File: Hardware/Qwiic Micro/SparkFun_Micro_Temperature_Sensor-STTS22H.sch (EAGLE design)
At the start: 26 parts, among them J1 Qwiic Right Angle, U2 STTS22H

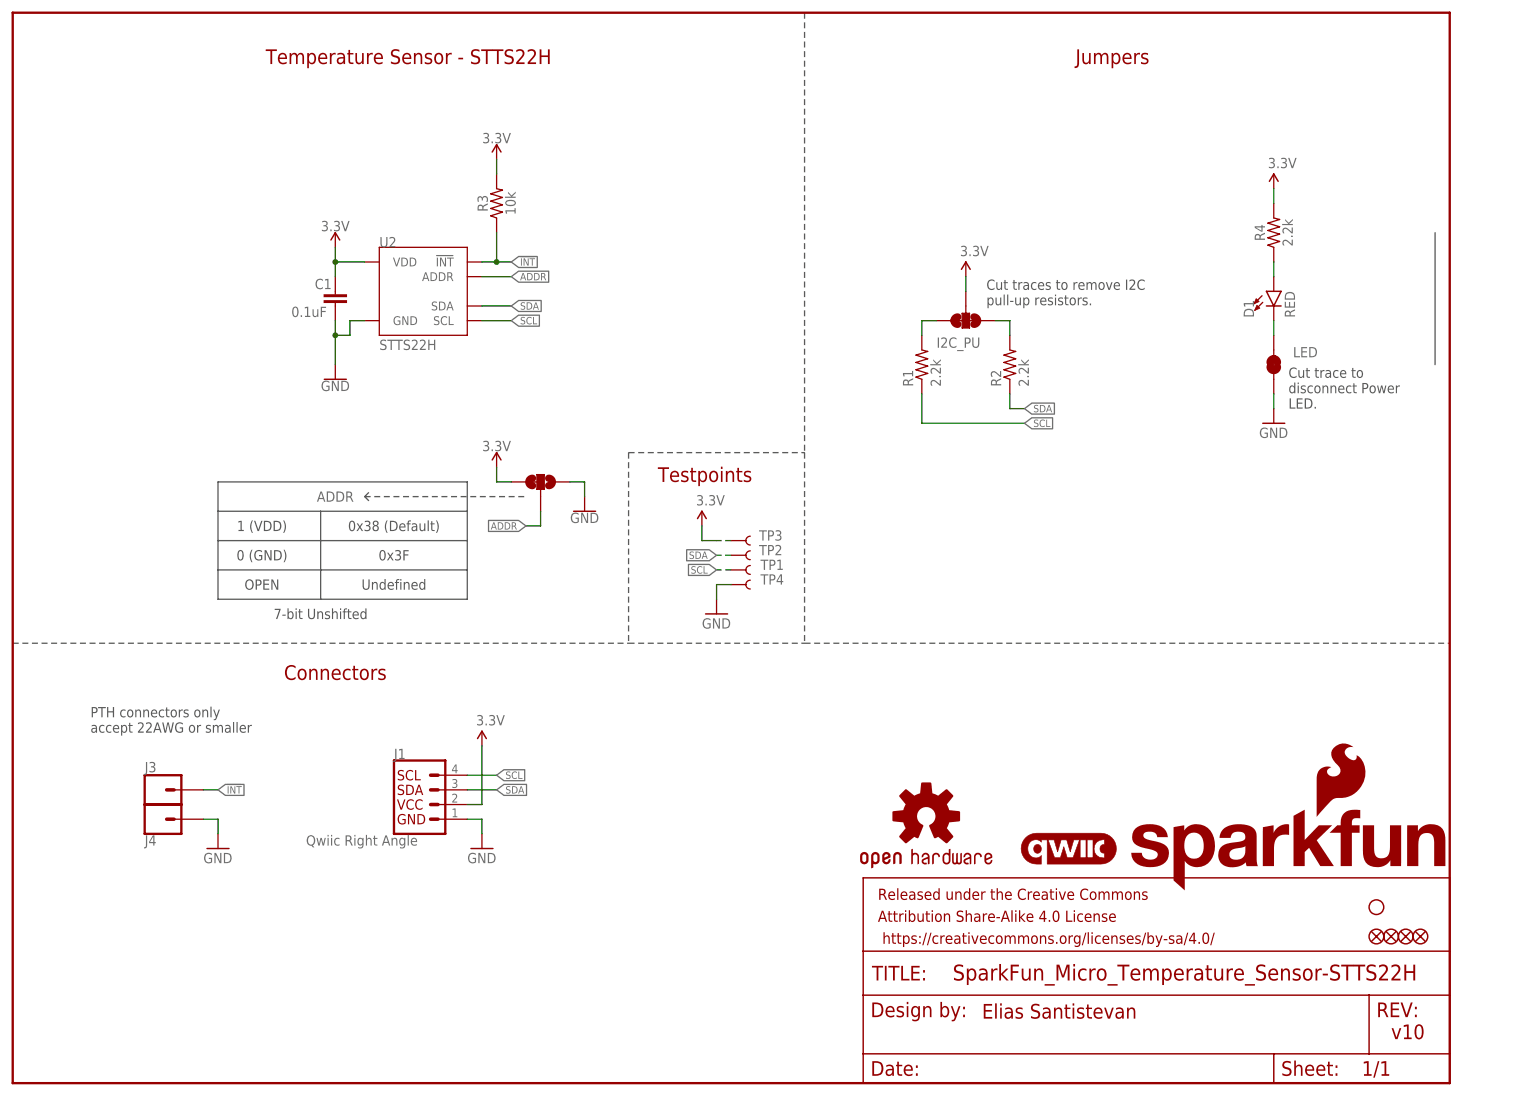
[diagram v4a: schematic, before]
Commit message: Updates temp sensor footprint, Adds bstop underneath IC
* Adds via directly underneath sensor for better temperature sensing
* Fixes various routing inconsistencies
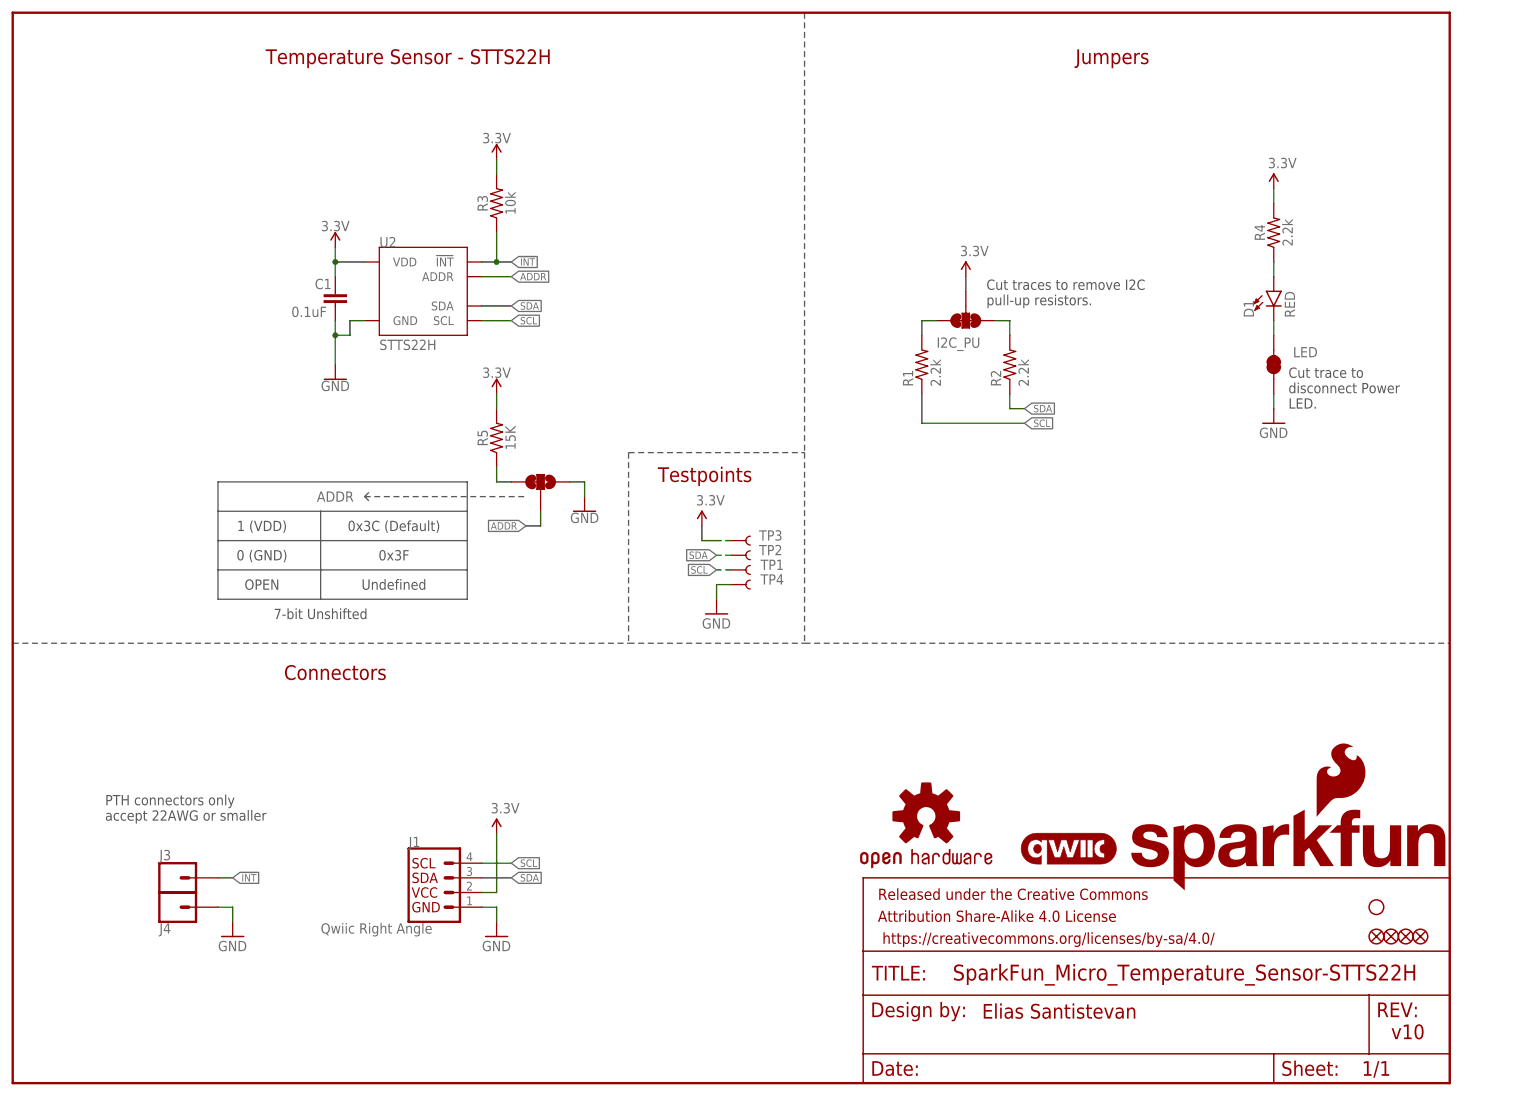
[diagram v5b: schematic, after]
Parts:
- added R5: 15K, SparkFun-Resistors:15KOHM-0402-TIGHT-1/16THW-1%
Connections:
- new net N$1: ADDR.3, R5.1
- net 3.3V: now also R5.2; no longer ADDR.3
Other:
- note added: "0x3C (Default)"
- note removed: "0x38 (Default)"
- moved on the sheet: J1, J3, J4
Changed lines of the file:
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@@
 <part name="GND5" library="SparkFun-PowerSymbols" deviceset="GND" device=""/>
 <part name="C1" library="SparkFun-Capacitors" deviceset="0.1UF" device="-0402T-16V-10%" value="0.1uF"/>
+<part name="R5" library="SparkFun-Resistors" deviceset="15KOHM" device="-0402-TIGHT-1/16THW-1%" value="15K"/>
 </parts>
 <sheets>
@@
 <text x="55.88" y="71.12" size="2.54" layer="94" font="vector" align="center">Connectors</text>
 <wire x1="137.16" y1="109.22" x2="137.16" y2="76.2" width="0.2032" layer="97" style="longdash"/>
-<wire x1="246.38" y1="124.46" x2="246.38" y2="147.32" width="0.2032" layer="97"/>
 <text x="167.894" y="11.176" size="2.54" layer="94" font="vector">Elias Santistevan</text>
 <wire x1="106.68" y1="109.22" x2="137.16" y2="109.22" width="0.2032" layer="97" style="longdash"/>
@@
 <wire x1="106.68" y1="109.22" x2="106.68" y2="76.2" width="0.2032" layer="97" style="longdash"/>
 <wire x1="106.68" y1="76.2" x2="137.16" y2="76.2" width="0.2032" layer="97" style="longdash"/>
-<text x="13.462" y="60.706" size="1.778" layer="97" font="vector">PTH connectors only
+<text x="16.002" y="45.466" size="1.778" layer="97" font="vector">PTH connectors only
 accept 22AWG or smaller</text>
 <wire x1="35.56" y1="104.14" x2="35.56" y2="99.06" width="0.1524" layer="97"/>
@@
 <wire x1="35.56" y1="93.98" x2="53.34" y2="93.98" width="0.1524" layer="97"/>
 <wire x1="53.34" y1="93.98" x2="78.74" y2="93.98" width="0.1524" layer="97"/>
-<text x="66.04" y="96.52" size="1.778" layer="97" font="vector" align="center">0x38 (Default)</text>
+<text x="66.04" y="96.52" size="1.778" layer="97" font="vector" align="center">0x3C (Default)</text>
 <text x="66.04" y="91.44" size="1.778" layer="97" font="vector" align="center">0x3F</text>
 <wire x1="60.96" y1="101.6" x2="88.9" y2="101.6" width="0.1524" layer="97" style="dashdot"/>
@@
 <attribute name="VALUE" x="215.9" y="111.76" size="1.778" layer="96" font="vector"/>
 </instance>
-<instance part="J1" gate="G$1" x="71.12" y="48.26" smashed="yes">
-<attribute name="VALUE" x="50.8" y="42.926" size="1.778" layer="96" font="vector" align="top-left"/>
-<attribute name="NAME" x="66.04" y="56.134" size="1.778" layer="95" font="vector"/>
-</instance>
-<instance part="GND3" gate="1" x="81.28" y="40.64" smashed="yes">
-<attribute name="VALUE" x="78.74" y="38.1" size="1.778" layer="96" font="vector"/>
-</instance>
-<instance part="SUPPLY1" gate="G$1" x="81.28" y="58.42" smashed="yes">
-<attribute name="VALUE" x="80.264" y="61.976" size="1.778" layer="96" font="vector"/>
+<instance part="J1" gate="G$1" x="73.66" y="33.02" smashed="yes">
+<attribute name="VALUE" x="53.34" y="27.686" size="1.778" layer="96" font="vector" align="top-left"/>
+<attribute name="NAME" x="68.58" y="40.894" size="1.778" layer="95" font="vector"/>
+</instance>
+<instance part="GND3" gate="1" x="83.82" y="25.4" smashed="yes">
+<attribute name="VALUE" x="81.28" y="22.86" size="1.778" layer="96" font="vector"/>
+</instance>
+<instance part="SUPPLY1" gate="G$1" x="83.82" y="43.18" smashed="yes">
+<attribute name="VALUE" x="82.804" y="46.736" size="1.778" layer="96" font="vector"/>
 </instance>
 <instance part="LOGO1" gate="G$1" x="182.88" y="40.64" smashed="yes"/>
@@
 <attribute name="VALUE" x="118.364" y="100.076" size="1.778" layer="96" font="vector"/>
 </instance>
-<instance part="J3" gate="G$1" x="25.4" y="50.8" smashed="yes">
-<attribute name="VALUE" x="22.86" y="45.974" size="1.778" layer="96" font="vector"/>
-<attribute name="NAME" x="22.86" y="53.848" size="1.778" layer="95" font="vector"/>
-</instance>
-<instance part="J4" gate="G$1" x="25.4" y="45.72" smashed="yes">
-<attribute name="VALUE" x="22.86" y="40.894" size="1.778" layer="96" font="vector"/>
-<attribute name="NAME" x="22.86" y="41.148" size="1.778" layer="95" font="vector"/>
-</instance>
-<instance part="GND2" gate="1" x="35.56" y="40.64" smashed="yes">
-<attribute name="VALUE" x="33.02" y="38.1" size="1.778" layer="96" font="vector"/>
+<instance part="J3" gate="G$1" x="27.94" y="35.56" smashed="yes">
+<attribute name="VALUE" x="25.4" y="30.734" size="1.778" layer="96" font="vector"/>
+<attribute name="NAME" x="25.4" y="38.608" size="1.778" layer="95" font="vector"/>
+</instance>
+<instance part="J4" gate="G$1" x="27.94" y="30.48" smashed="yes">
+<attribute name="VALUE" x="25.4" y="25.654" size="1.778" layer="96" font="vector"/>
+<attribute name="NAME" x="25.4" y="25.908" size="1.778" layer="95" font="vector"/>
+</instance>
+<instance part="GND2" gate="1" x="38.1" y="25.4" smashed="yes">
+<attribute name="VALUE" x="35.56" y="22.86" size="1.778" layer="96" font="vector"/>
 </instance>
 <instance part="TP4" gate="G$1" x="124.46" y="86.36" smashed="yes">
@@
 <attribute name="NAME" x="55.88" y="101.6" size="1.778" layer="95" font="vector" rot="MR0" align="center"/>
 </instance>
-<instance part="SUPPLY8" gate="G$1" x="83.82" y="106.68" smashed="yes">
-<attribute name="VALUE" x="83.82" y="109.474" size="1.778" layer="96" font="vector" align="bottom-center"/>
+<instance part="SUPPLY8" gate="G$1" x="83.82" y="119.38" smashed="yes">
+<attribute name="VALUE" x="83.82" y="122.174" size="1.778" layer="96" font="vector" align="bottom-center"/>
 </instance>
 <instance part="GND5" gate="1" x="99.06" y="99.06" smashed="yes">
@@
 <attribute name="NAME" x="52.324" y="137.541" size="1.778" layer="95" font="vector"/>
 <attribute name="VALUE" x="48.26" y="132.715" size="1.778" layer="96" font="vector"/>
+</instance>
+<instance part="R5" gate="G$1" x="83.82" y="111.76" smashed="yes" rot="R90">
+<attribute name="NAME" x="82.296" y="111.76" size="1.778" layer="95" font="vector" rot="R90" align="bottom-center"/>
+<attribute name="VALUE" x="85.344" y="111.76" size="1.778" layer="96" font="vector" rot="R90" align="top-center"/>
 </instance>
 </instances>
@@
 <segment>
 <pinref part="J1" gate="G$1" pin="1"/>
-<wire x1="78.74" y1="45.72" x2="81.28" y2="45.72" width="0.1524" layer="91"/>
-<wire x1="81.28" y1="45.72" x2="81.28" y2="43.18" width="0.1524" layer="91"/>
+<wire x1="81.28" y1="30.48" x2="83.82" y2="30.48" width="0.1524" layer="91"/>
+<wire x1="83.82" y1="30.48" x2="83.82" y2="27.94" width="0.1524" layer="91"/>
 <pinref part="GND3" gate="1" pin="GND"/>
 </segment>
 <segment>
-<wire x1="33.02" y1="45.72" x2="35.56" y2="45.72" width="0.1524" layer="91"/>
-<wire x1="35.56" y1="45.72" x2="35.56" y2="43.18" width="0.1524" layer="91"/>
+<wire x1="35.56" y1="30.48" x2="38.1" y2="30.48" width="0.1524" layer="91"/>
+<wire x1="38.1" y1="30.48" x2="38.1" y2="27.94" width="0.1524" layer="91"/>
 <pinref part="GND2" gate="1" pin="GND"/>
 <pinref part="J4" gate="G$1" pin="1"/>
@@
 <segment>
 <pinref part="J1" gate="G$1" pin="4"/>
-<wire x1="78.74" y1="53.34" x2="83.82" y2="53.34" width="0.1524" layer="91"/>
-<label x="83.82" y="53.34" size="1.27" layer="95" font="vector" xref="yes"/>
+<wire x1="81.28" y1="38.1" x2="86.36" y2="38.1" width="0.1524" layer="91"/>
+<label x="86.36" y="38.1" size="1.27" layer="95" font="vector" xref="yes"/>
 </segment>
 <segment>
@@
 <segment>
 <pinref part="J1" gate="G$1" pin="3"/>
-<wire x1="78.74" y1="50.8" x2="83.82" y2="50.8" width="0.1524" layer="91"/>
-<label x="83.82" y="50.8" size="1.27" layer="95" font="vector" xref="yes"/>
+<wire x1="81.28" y1="35.56" x2="86.36" y2="35.56" width="0.1524" layer="91"/>
+<label x="86.36" y="35.56" size="1.27" layer="95" font="vector" xref="yes"/>
 </segment>
 <segment>
@@
 <segment>
 <pinref part="J1" gate="G$1" pin="2"/>
-<wire x1="78.74" y1="48.26" x2="81.28" y2="48.26" width="0.1524" layer="91"/>
-<wire x1="81.28" y1="48.26" x2="81.28" y2="58.42" width="0.1524" layer="91"/>
+<wire x1="81.28" y1="33.02" x2="83.82" y2="33.02" width="0.1524" layer="91"/>
+<wire x1="83.82" y1="33.02" x2="83.82" y2="43.18" width="0.1524" layer="91"/>
 <pinref part="SUPPLY1" gate="G$1" pin="3.3V"/>
 </segment>
@@
 </segment>
 <segment>
-<pinref part="ADDR" gate="G$1" pin="3"/>
-<wire x1="86.36" y1="104.14" x2="83.82" y2="104.14" width="0.1524" layer="91"/>
-<wire x1="83.82" y1="104.14" x2="83.82" y2="106.68" width="0.1524" layer="91"/>
+<pinref part="R5" gate="G$1" pin="2"/>
 <pinref part="SUPPLY8" gate="G$1" pin="3.3V"/>
+<wire x1="83.82" y1="116.84" x2="83.82" y2="119.38" width="0.1524" layer="91"/>
 </segment>
 </net>
@@
 </segment>
 <segment>
-<wire x1="33.02" y1="50.8" x2="35.56" y2="50.8" width="0.1524" layer="91"/>
-<label x="35.56" y="50.8" size="1.27" layer="95" font="vector" xref="yes"/>
+<wire x1="35.56" y1="35.56" x2="38.1" y2="35.56" width="0.1524" layer="91"/>
+<label x="38.1" y="35.56" size="1.27" layer="95" font="vector" xref="yes"/>
 <pinref part="J3" gate="G$1" pin="1"/>
 </segment>
@@
 </segment>
 </net>
+<net name="N$1" class="0">
+<segment>
+<pinref part="ADDR" gate="G$1" pin="3"/>
+<wire x1="86.36" y1="104.14" x2="83.82" y2="104.14" width="0.1524" layer="91"/>
+<pinref part="R5" gate="G$1" pin="1"/>
+<wire x1="83.82" y1="106.68" x2="83.82" y2="104.14" width="0.1524" layer="91"/>
+</segment>
+</net>

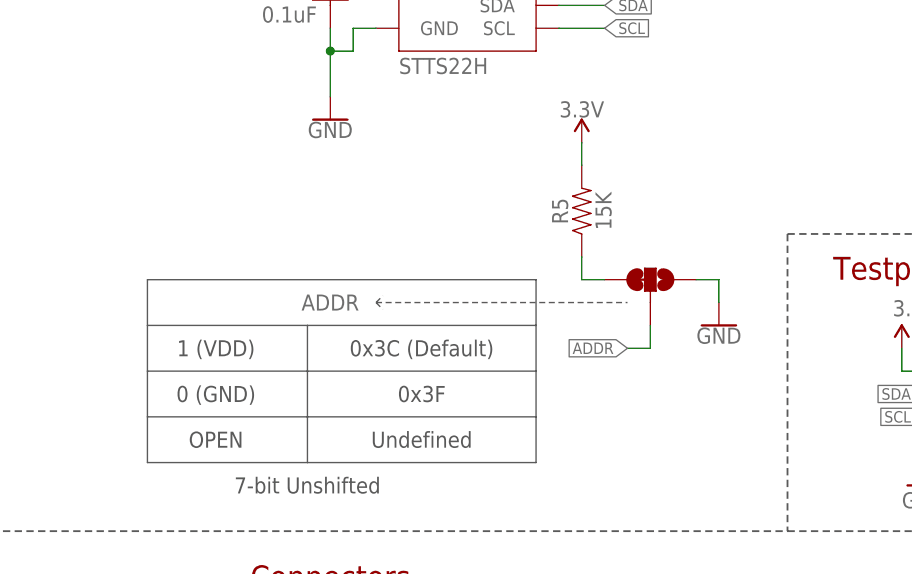
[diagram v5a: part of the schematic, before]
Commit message: Moves address selection around to be more clear in the schematic
* Changes second address option on micro to 3v3 instead of GND
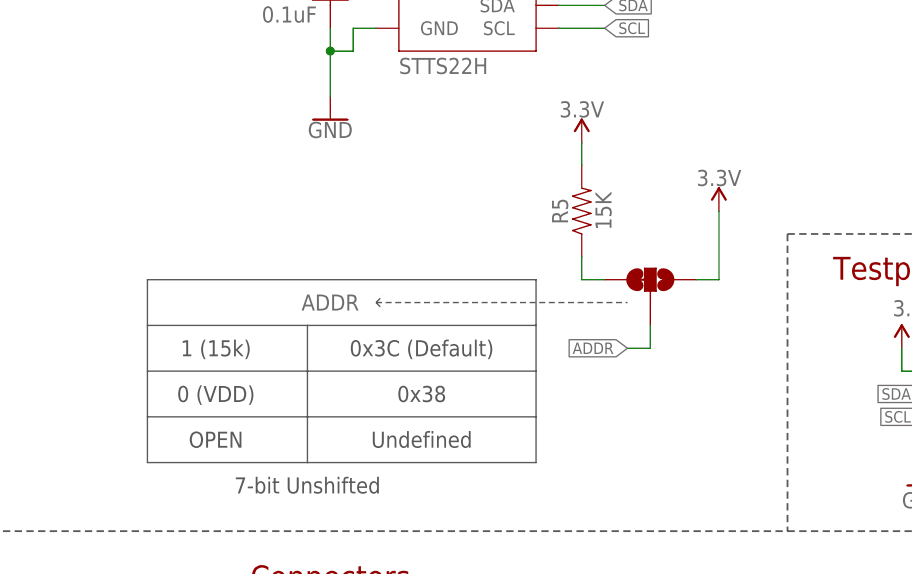
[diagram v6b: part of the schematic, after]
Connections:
- net 3.3V: now also ADDR.1
- net GND: no longer ADDR.1
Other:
- note added: "0 (VDD)"
- note added: "0x38"
- note added: "1 (15k)"
- note removed: "0 (GND)"
- note removed: "0x3F"
- note removed: "1 (VDD)"
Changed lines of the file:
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@@
 <part name="ADDR" library="SparkFun-Jumpers" deviceset="JUMPER-SMT_3_1-NC_TRACE" device="_SILK" package3d_urn="urn:adsk.eagle:package:39288/1"/>
 <part name="SUPPLY8" library="SparkFun-PowerSymbols" deviceset="3.3V" device=""/>
-<part name="GND5" library="SparkFun-PowerSymbols" deviceset="GND" device=""/>
 <part name="C1" library="SparkFun-Capacitors" deviceset="0.1UF" device="-0402T-16V-10%" value="0.1uF"/>
 <part name="R5" library="SparkFun-Resistors" deviceset="15KOHM" device="-0402-TIGHT-1/16THW-1%" value="15K"/>
+<part name="SUPPLY7" library="SparkFun-PowerSymbols" deviceset="3.3V" device=""/>
 </parts>
 <sheets>
@@
 <wire x1="35.56" y1="83.82" x2="53.34" y2="83.82" width="0.1524" layer="97"/>
 <wire x1="53.34" y1="88.9" x2="78.74" y2="88.9" width="0.1524" layer="97"/>
-<text x="43.18" y="96.52" size="1.778" layer="97" font="vector" align="center">1 (VDD)</text>
-<text x="43.18" y="91.44" size="1.778" layer="97" font="vector" align="center">0 (GND)</text>
+<text x="43.18" y="96.52" size="1.778" layer="97" font="vector" align="center">1 (15k)</text>
+<text x="43.18" y="91.44" size="1.778" layer="97" font="vector" align="center">0 (VDD)</text>
 <text x="43.18" y="86.36" size="1.778" layer="97" font="vector" align="center">OPEN</text>
 <text x="66.04" y="86.36" size="1.778" layer="97" font="vector" align="center">Undefined</text>
@@
 <wire x1="53.34" y1="93.98" x2="78.74" y2="93.98" width="0.1524" layer="97"/>
 <text x="66.04" y="96.52" size="1.778" layer="97" font="vector" align="center">0x3C (Default)</text>
-<text x="66.04" y="91.44" size="1.778" layer="97" font="vector" align="center">0x3F</text>
+<text x="66.04" y="91.44" size="1.778" layer="97" font="vector" align="center">0x38</text>
 <wire x1="60.96" y1="101.6" x2="88.9" y2="101.6" width="0.1524" layer="97" style="dashdot"/>
 <wire x1="60.96" y1="101.6" x2="61.722" y2="102.362" width="0.1524" layer="97" style="dashdot"/>
@@
 <attribute name="VALUE" x="83.82" y="122.174" size="1.778" layer="96" font="vector" align="bottom-center"/>
 </instance>
-<instance part="GND5" gate="1" x="99.06" y="99.06" smashed="yes">
-<attribute name="VALUE" x="99.06" y="98.806" size="1.778" layer="96" font="vector" align="top-center"/>
-</instance>
 <instance part="C1" gate="G$1" x="55.88" y="134.62" smashed="yes">
 <attribute name="NAME" x="52.324" y="137.541" size="1.778" layer="95" font="vector"/>
@@
 <attribute name="NAME" x="82.296" y="111.76" size="1.778" layer="95" font="vector" rot="R90" align="bottom-center"/>
 <attribute name="VALUE" x="85.344" y="111.76" size="1.778" layer="96" font="vector" rot="R90" align="top-center"/>
+</instance>
+<instance part="SUPPLY7" gate="G$1" x="99.06" y="111.76" smashed="yes">
+<attribute name="VALUE" x="99.06" y="114.554" size="1.778" layer="96" font="vector" align="bottom-center"/>
 </instance>
 </instances>
@@
 <junction x="55.88" y="129.54"/>
 </segment>
-<segment>
-<pinref part="ADDR" gate="G$1" pin="1"/>
-<wire x1="96.52" y1="104.14" x2="99.06" y2="104.14" width="0.1524" layer="91"/>
-<wire x1="99.06" y1="104.14" x2="99.06" y2="101.6" width="0.1524" layer="91"/>
-<pinref part="GND5" gate="1" pin="GND"/>
-</segment>
 </net>
 <net name="SCL" class="0">
@@
 <wire x1="83.82" y1="116.84" x2="83.82" y2="119.38" width="0.1524" layer="91"/>
 </segment>
+<segment>
+<pinref part="ADDR" gate="G$1" pin="1"/>
+<wire x1="96.52" y1="104.14" x2="99.06" y2="104.14" width="0.1524" layer="91"/>
+<wire x1="99.06" y1="104.14" x2="99.06" y2="111.76" width="0.1524" layer="91"/>
+<pinref part="SUPPLY7" gate="G$1" pin="3.3V"/>
+</segment>
 </net>
